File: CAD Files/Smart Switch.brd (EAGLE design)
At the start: 88.6 x 63.4 mm, 20 parts, among them K1 G5L, X3 MKDSN1,5/4-5,08

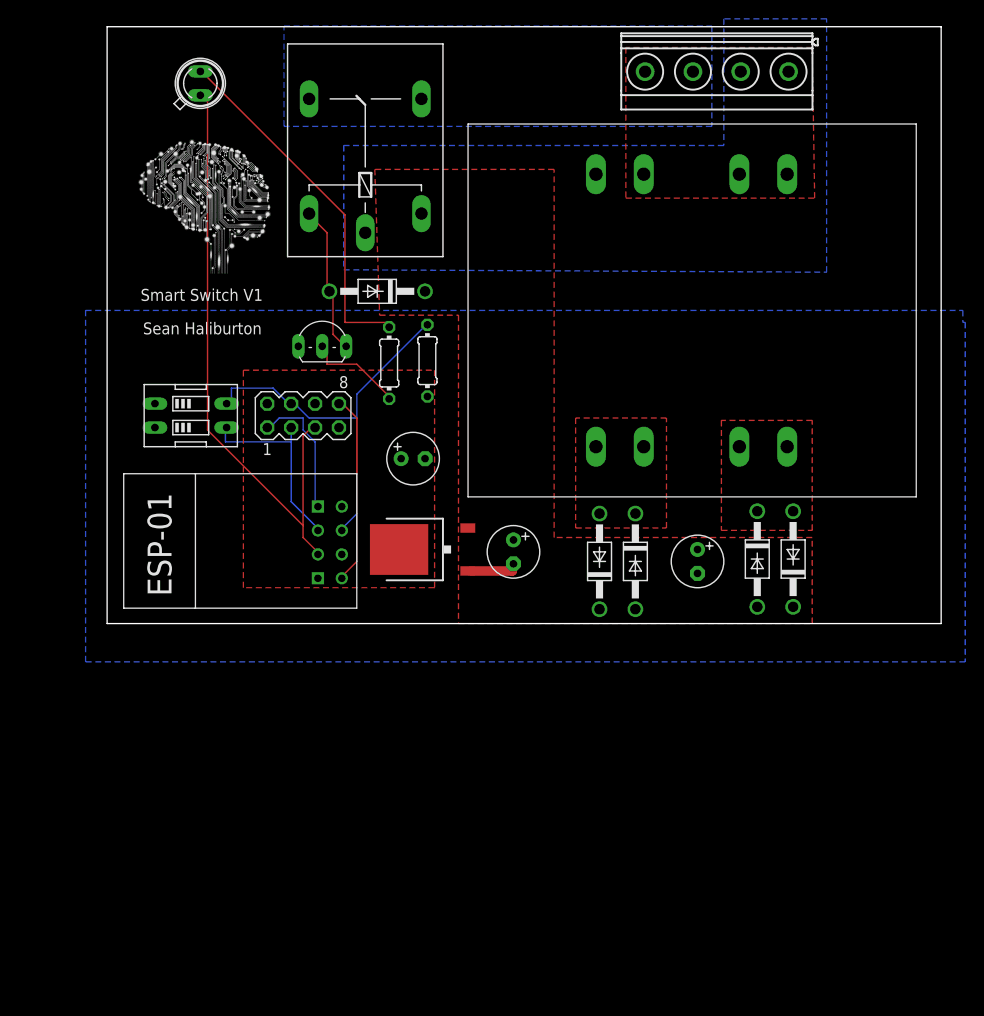
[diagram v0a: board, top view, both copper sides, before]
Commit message: Revision was sent for manufacturing
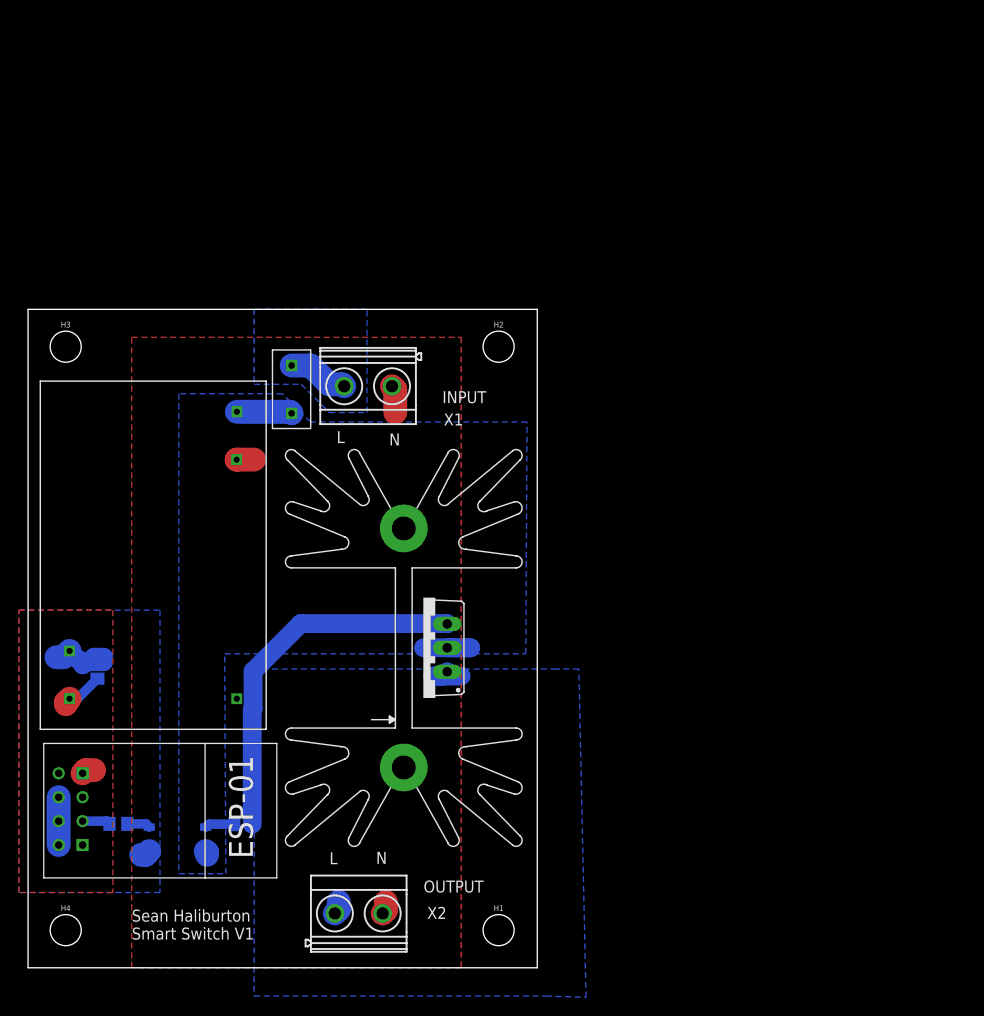
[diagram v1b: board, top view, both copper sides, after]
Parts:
- removed C2: 470u, resistor:E2,5-6
- removed C3: 10u, resistor:E2,5-6
- removed D1, D3, D4, D5, D6: 1N4004, diode:DO41-10
- removed D2: SFH482, led:SFH482
- removed SV1: (no value), con-lstb:MA04-2
- removed SW1: (no value), special:EDG-02
- removed T1: (no value), transistor-neu-to92:TO92-EBC
- removed X3: MKDSN1,5/4-5,08, con-phoenix-508:MKDSN1,5/4-5,08
- added H1, H2, H3, H4: STAND-OFF, SparkFun-Hardware:STAND-OFF
- added U$5: RA-T2X-38E, smart-switch:SK129
- added X1, X2: MKDSN1,5/2-5,08, con-phoenix-508:MKDSN1,5/2-5,08
- C1: device resistor:E2,5-6 -> resistor:C0805
- K1: value G5L -> ATP1211SX; device relay:G5LE -> relay:SOP04
- R1: value 10k -> 100; device rcl:0204/7 -> resistor:R0805
- R2: value 2k2 -> 200; device rcl:0204/7 -> resistor:R0805
- U$2: value ZLDO1117 -> RAC04-GB; device smart-switch:TO252 -> smart-switch:RAC04-GB
- U$3: value CL2-10R-12 -> BTA16; device smart-switch:TRANSFORMER -> smart-switch:TO220V
- U$4: value (none) -> FUSE; device smart-switch:BRAIN -> smart-switch:FUSE
- moved U$3 81.3 mm to (42.0, 34.0), turned to 90 degrees
- moved K1 76.6 mm to (15.9, 13.7), flipped to the bottom
- moved R1 59.2 mm to (9.58, 15.3), flipped to the bottom, turned to 0 degrees
- moved R2 51.4 mm to (22.9, 15.3), flipped to the bottom, turned to 180 degrees
- moved U$2 40.7 mm to (4.39, 28.6), turned to 270 degrees
- moved C1 40.4 mm to (7.35, 31.7), flipped to the bottom, turned to 270 degrees
- moved U$1 31.5 mm to (11.4, 16.8), turned to 270 degrees
- moved U$4 11.4 mm to (28.0, 64.0), turned to 270 degrees
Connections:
- removed net 3.3V: C1.+, R1.2, SV1.2, SV1.6, U$1.CH_PD, U$1.VCC, U$2.3
- removed net DC+: C2.+, C3.+, D1.C, D3.C, D4.C, K1.1, U$2.2
- removed net GPIO2: D2.A, SV1.5, U$1.GPIO2
- removed net N$3: D1.A, K1.2, T1.C
- removed net RESET: R1.1, SV1.4, SW1.4, U$1.RST
- removed net RXD: SV1.1, U$1.RX
- removed net SEC1: D3.A, D6.C, U$3.12
- removed net SEC2: D4.A, D5.C, U$3.7
- removed net TXD: SV1.8, U$1.TX
- new net L_IN: U$4.P$1, X1.2
- new net N$6: R2.2, U$3.3
- new net VCC: C1.1, K1.1, U$1.CH_PD, U$1.RST, U$1.VCC, U$2.3.3
- net GND: now also C1.2, U$2.GND; no longer C1.-, C2.-, C3.-, D5.A, D6.A, SV1.7, SW1.1, SW1.2, T1.E, U$2.1
- net GPIO0: now also R1.2; no longer SV1.3, SW1.3
- net LIVE: now also K1.4, U$2.L, U$3.2, U$4.P$2; no longer K1.P, U$3.3, U$3.6, X3.2
- net N$1: now also K1.2, R1.1; no longer R2.1, T1.B
- net N$5: now also K1.3, R2.1; no longer D2.K, R2.2
- net NEUTRAL: now also U$2.N, X1.1, X2.2; no longer U$3.1, U$3.4, X3.1, X3.4
- net SWITCH: now also U$3.1, X2.1; no longer K1.O, X3.3
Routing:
- net GPIO2: track 65.7 -> 0.00 mm
- net RESET: track 42.6 -> 0.00 mm
- net N$6: track 0.00 -> 39.0 mm
- net N$5: track 38.1 -> 3.17 mm
- net TXD: track 20.7 -> 0.00 mm
- net GPIO0: track 20.6 -> 2.98 mm
- net N$3: track 15.9 -> 0.00 mm
- net RXD: track 14.5 -> 0.00 mm
- net VCC: track 0.00 -> 14.2 mm
- net LIVE: track 0.00 -> 13.8 mm
- net N$1: track 10.6 -> 2.47 mm
- net L_IN: track 0.00 -> 6.50 mm
- net NEUTRAL: track 0.00 -> 6.16 mm
- net SWITCH: track 0.00 -> 6.11 mm
- net GND: track 5.36 -> 5.96 mm
- added copper zone on layer 1, net GND
- added copper zone on layer 16, net L_IN
- added copper zone on layer 16, net VCC
- removed copper zone on layer 1, net 3.3V
- removed copper zone on layer 1, net DC+
- removed copper zone on layer 16, net GND
- removed copper zone on layer 1, net SEC1
- removed copper zone on layer 1, net SEC2
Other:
- board size 88.6 x 63.4 mm -> 54.1 x 70 mm
- board text added: "INPUT"
- board text added: "L"
- board text added: "N"
- board text added: "OUTPUT"
- board text added: "Sean Haliburton Smart Switch V1"
- board text removed: "Sean Haliburton"
- board text removed: "Smart Switch V1"
